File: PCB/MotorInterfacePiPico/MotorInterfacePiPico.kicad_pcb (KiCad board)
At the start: 2 copper layers, 120.2 x 65.5 mm, 47 parts, among them J1 Motor Connector, J2 Screw_Terminal_01x06, Q1 2N3904, Q2 2N3904, Q3 2N3904, U1 Pico, U2 OPA4197, U3 LM7810, U4 LM79L05

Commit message: PCB layout complete, need to DNC, need BOM
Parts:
- added G***: LOGO, TJR:gnome, B.Cu at (122.3, 105.8)
- added REF**: TNT, TSL:TNT, F.Cu at (122.2, 62.8)
- added REF**: BennyHead, TSL:BennyHead, F.Cu at (158.5, 83.0)
- added REF**: BennySmall, TSL:BennySmall, F.Cu at (162.5, 87.2)
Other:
- board text added: "A"
- board text added: "B"
- board text added: "E+"
- board text added: "E-"
- board text added: "Gnd"
- board text added: "Lim"
- board text added: "M+"
- board text added: "M-"
- board text added: "P10x"
- board text added: "Pos"
- board text added: "Spd"
- board text added: "V+"

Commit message: Layout complete, need BOM
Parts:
- U2: footprint Package_SO:SOIC-14_3.9x8.7mm_P1.27mm -> TJR:D14_TEX
- moved REF** 28.6 mm to (99.8, 80.5)
- moved G*** 23.7 mm to (99.7, 98.4)
- moved REF** 15.4 mm to (143.1, 82.8)
- moved REF** 0.66 mm to (162.7, 86.6)

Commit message: add gerbers, need BOM
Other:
- board text added: "0.0000 mm / 0.0000 mm"
- board text added: "0.3000 mm"
- board text added: "1.6000 mm"
- board text added: "120.2500 mm x 65.5000 mm"
- board text added: "2"
- board text added: "BOARD CHARACTERISTICS"
- board text added: "Board Thickness:"
- board text added: "Board overall dimensions:"
- board text added: "Castellated pads:"
- board text added: "Copper Finish:"
- board text added: "Copper Layer Count:"
- board text added: "Edge card connectors:"
- board text added: "Impedance Control:"
- board text added: "Min hole diameter:"
- board text added: "Min track/spacing:"
- board text added: "No"
- board text added: "None"
- board text added: "Plated Board Edge:"

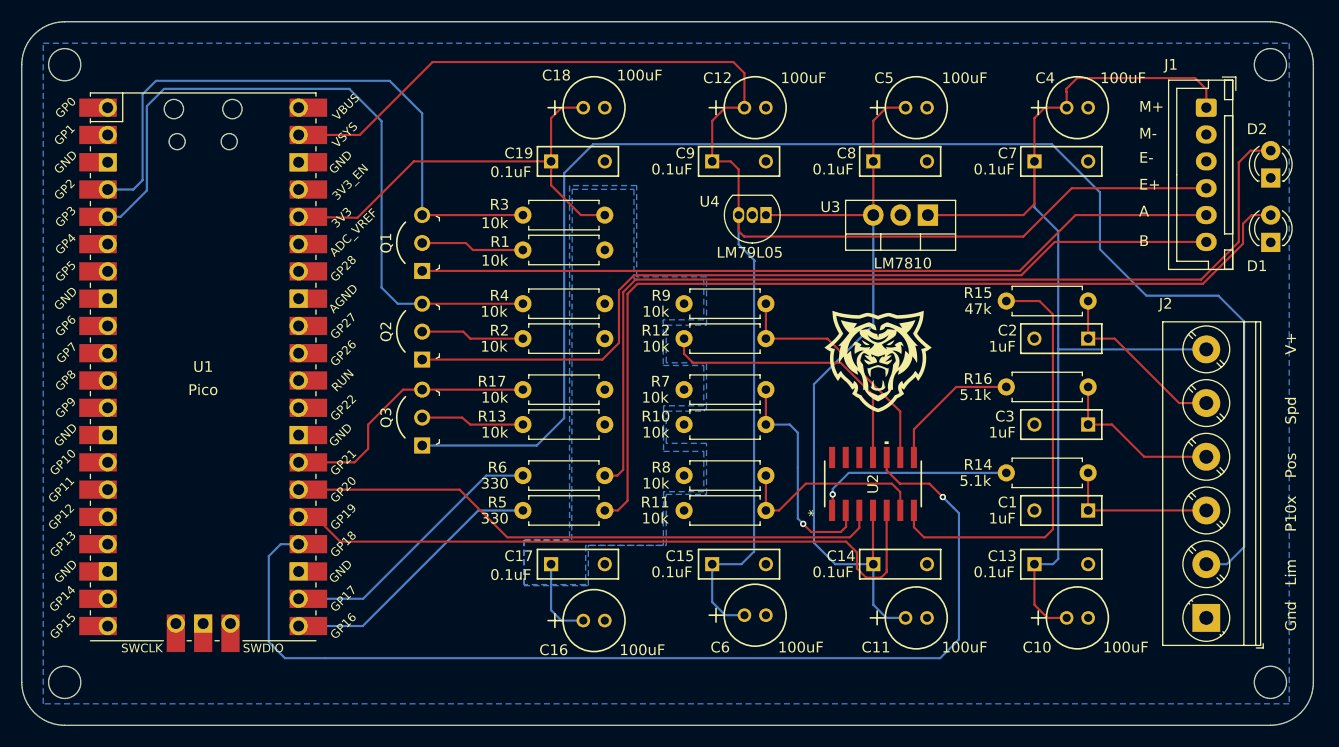
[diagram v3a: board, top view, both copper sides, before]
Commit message: Surface Mount Board design
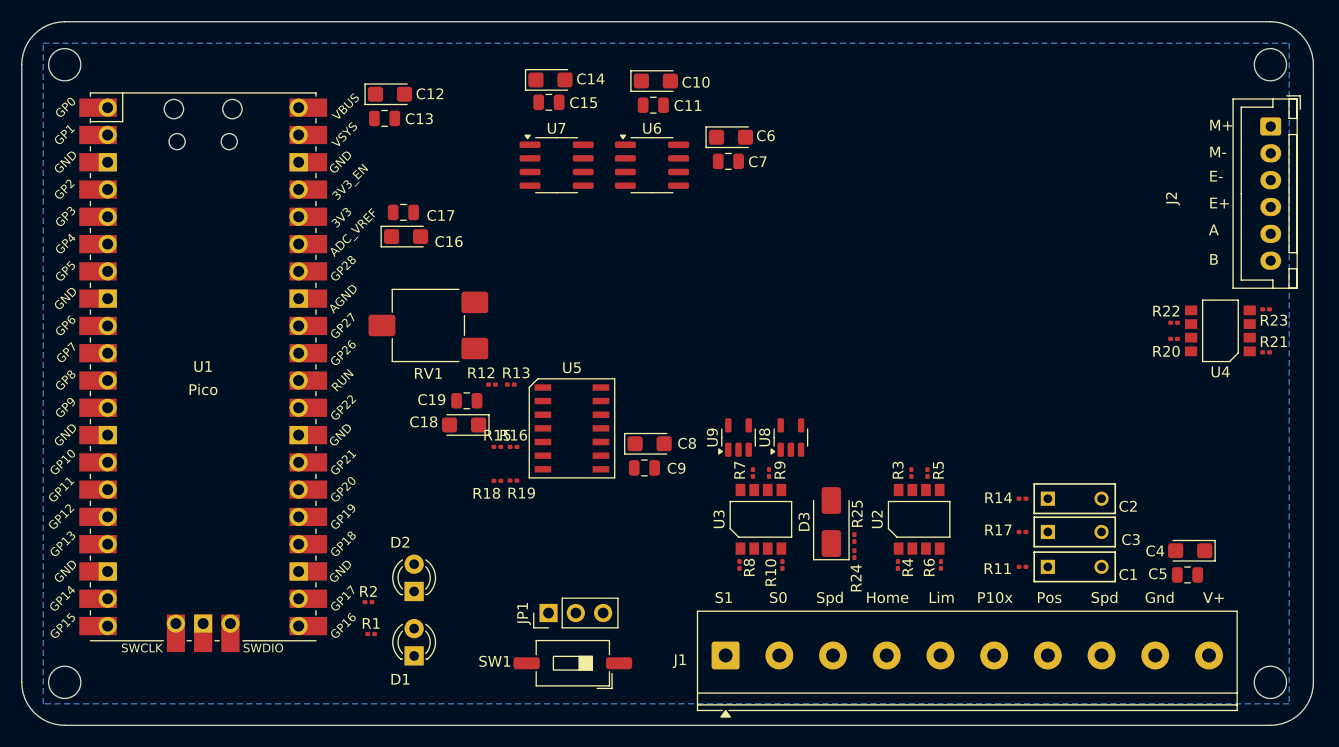
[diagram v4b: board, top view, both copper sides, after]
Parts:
- removed Q1, Q2, Q3: 2N3904, TJR:TO-92-3_Formed_Leads
- removed REF**: BennyHead, TSL:BennyHead
- removed REF**: BennySmall, TSL:BennySmall
- removed REF**: TNT, TSL:TNT
- added D3: 3.6V, Diode_SMD:D_SMA, F.Cu at (158.4, 101.6)
- added JP1: Jumper_3_Bridged12, Connector_PinHeader_2.54mm:PinHeader_1x03_P2.54mm_Vertical, F.Cu at (132.0, 110.0)
- added R18: 10k, Resistor_SMD:R_0201_0603Metric, F.Cu at (127.3, 97.7)
- added R19: 10k, Resistor_SMD:R_0201_0603Metric, F.Cu at (128.8, 97.7)
- added R20: 10k, Resistor_SMD:R_0201_0603Metric, F.Cu at (190.3, 84.5)
- added R21: 4.7k, Resistor_SMD:R_0201_0603Metric, F.Cu at (198.8, 85.8)
- added R22: 10k, Resistor_SMD:R_0201_0603Metric, F.Cu at (190.3, 83.0)
- added R23: 4.7k, Resistor_SMD:R_0201_0603Metric, F.Cu at (198.8, 81.8)
- added R24: 6.2k, Resistor_SMD:R_0201_0603Metric, F.Cu at (160.5, 104.6)
- added R25: 13k, Resistor_SMD:R_0201_0603Metric, F.Cu at (160.5, 103.1)
- added RV1: 10k, Potentiometer_SMD:Potentiometer_ACP_CA6-VSMD_Vertical, F.Cu at (120.9, 83.3)
- added SW1: SW_DIP_x01, Button_Switch_SMD:SW_DIP_SPSTx01_Slide_6.7x4.1mm_W8.61mm_P2.54mm_LowProfile, F.Cu at (134.3, 114.7)
- added U5: OPA4197, CustomBPA:SO-14_5.4_P1.27, F.Cu at (134.2, 92.9)
- added U6: LM7810, Package_SO:SOIC-8_3.9x4.9mm_P1.27mm, F.Cu at (141.7, 68.4)
- added U7: LM78L05_SO8, Package_SO:SOIC-8_3.9x4.9mm_P1.27mm, F.Cu at (132.8, 68.4)
- added U8: 74LVC1G08GV, Package_TO_SOT_SMD:SOT-23-5, F.Cu at (154.6, 93.7)
- added U9: 74LVC1G08GV, Package_TO_SOT_SMD:SOT-23-5, F.Cu at (149.7, 93.7)
- C10, C12, C16, C18, C4, C6: footprint TJR:C_Radial_D5.00mm_H12.5mm_P2.00mm -> Capacitor_Tantalum_SMD:CP_EIA-3216-10_Kemet-I
- C11, C5: value 100uF -> 0.1uF; footprint TJR:C_Radial_D5.00mm_H12.5mm_P2.00mm -> Capacitor_SMD:C_0805_2012Metric
- C13, C15, C17, C19, C7, C9: footprint TJR:C_Rect_L7.3mm_W2.5_H6.5mm_P5.0mm -> Capacitor_SMD:C_0805_2012Metric
- C14, C8: value 0.1uF -> 100uF; footprint TJR:C_Rect_L7.3mm_W2.5_H6.5mm_P5.0mm -> Capacitor_Tantalum_SMD:CP_EIA-3216-10_Kemet-I
- J1: value Motor Connector -> Screw_Terminal_01x10; footprint Connector_JST:JST_XH_B6B-XH-A_1x06_P2.50mm_Vertical -> TerminalBlock_Phoenix:TerminalBlock_Phoenix_PT-1,5-10-5.0-H_1x10_P5.00mm_Horizontal
- J2: value Screw_Terminal_01x06 -> Motor Connector; footprint TerminalBlock_Phoenix:TerminalBlock_Phoenix_PT-1,5-6-5.0-H_1x06_P5.00mm_Horizontal -> Connector_JST:JST_XH_B6B-XH-A_1x06_P2.50mm_Vertical
- R1, R2: value 10k -> 330; footprint TJR:R_Axial_DIN0207_L6.3mm_D2.5mm_P7.62mm_Horizontal -> Resistor_SMD:R_0201_0603Metric
- R10, R4, R8: value 10k -> 4.7k; footprint TJR:R_Axial_DIN0207_L6.3mm_D2.5mm_P7.62mm_Horizontal -> Resistor_SMD:R_0201_0603Metric
- R11, R17: value 10k -> 5.1k; footprint TJR:R_Axial_DIN0207_L6.3mm_D2.5mm_P7.62mm_Horizontal -> Resistor_SMD:R_0201_0603Metric
- R12, R13, R3, R7, R9: footprint TJR:R_Axial_DIN0207_L6.3mm_D2.5mm_P7.62mm_Horizontal -> Resistor_SMD:R_0201_0603Metric
- R14: value 5.1k -> 47k; footprint TJR:R_Axial_DIN0207_L6.3mm_D2.5mm_P7.62mm_Horizontal -> Resistor_SMD:R_0201_0603Metric
- R15: value 47k -> 10k; footprint TJR:R_Axial_DIN0207_L6.3mm_D2.5mm_P7.62mm_Horizontal -> Resistor_SMD:R_0201_0603Metric
- R16: value 5.1k -> 10k; footprint TJR:R_Axial_DIN0207_L6.3mm_D2.5mm_P7.62mm_Horizontal -> Resistor_SMD:R_0201_0603Metric
- R5: value 330 -> 10k; footprint TJR:R_Axial_DIN0207_L6.3mm_D2.5mm_P7.62mm_Horizontal -> Resistor_SMD:R_0201_0603Metric
- R6: value 330 -> 4.7k; footprint TJR:R_Axial_DIN0207_L6.3mm_D2.5mm_P7.62mm_Horizontal -> Resistor_SMD:R_0201_0603Metric
- U2: value OPA4197 -> ILD217T; footprint TJR:D14_TEX -> CustomBPA:SOIC-8_5.46mm_P1.27
- U3: value LM7810 -> ILD217T; footprint Package_TO_SOT_THT:TO-220-3_Vertical -> CustomBPA:SOIC-8_5.46mm_P1.27
- U4: value LM79L05 -> ILD217T; footprint Package_TO_SOT_THT:TO-92_Inline -> CustomBPA:SOIC-8_5.46mm_P1.27
- moved D1 88.6 mm to (119.5, 114.0)
- moved D2 88.6 mm to (119.5, 108.0)
- moved C13 73.4 mm to (116.8, 64.0)
- moved J1 67.8 mm to (148.5, 114.0), turned to 0 degrees
- moved C10 62.9 mm to (142.0, 60.5)
- moved C14 54.2 mm to (132.2, 60.4)
- moved C11 53.2 mm to (141.8, 62.8)
- moved C5 50.8 mm to (191.5, 106.5), turned to 180 degrees
- moved R15 49.3 mm to (127.3, 94.6)
- moved R16 46.2 mm to (128.8, 94.6)
- moved J2 46.1 mm to (199.3, 64.8), turned to -90 degrees
- moved C15 45.6 mm to (132.1, 62.5)
- moved C6 44.5 mm to (149.0, 65.8)
- moved U4 43.7 mm to (194.6, 83.8), turned to 90 degrees
- moved C4 42.8 mm to (191.8, 104.2), turned to 180 degrees
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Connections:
- C10 pad 1: +12V -> +10V
- C13 pad 1: +12V -> +5V
- C14 pad 1: +10V -> +5V
- C4 pad 1: +12V -> +Motor_Sup
- C5 pad 1: +10V -> +Motor_Sup
- C6 pad 1: +5V -> +Motor_Sup
- C7 pad 1: +12V -> +Motor_Sup
- C9 pad 1: +5V -> +10V
- J1 pad 1: +12V -> Net-(J1-Pin_1)
- J1 pad 2: GND -> Net-(J1-Pin_2)
- J1 pad 3: GND -> Speed Set
- J1 pad 4: +5V -> Net-(J1-Pin_4)
- J1 pad 5: A -> Net-(J1-Pin_5)
- J1 pad 6: B -> Analog Position x10
- J2 pad 1: GND -> M+
- J2 pad 2: Net-(J2-Pin_2) -> GND
- J2 pad 3: Analog Position x10 -> GND
- J2 pad 4: Analog Position -> +5V
- J2 pad 5: Analog Speed -> Net-(J2-Pin_5)
- J2 pad 6: +12V -> Net-(J2-Pin_6)
- R1 pad 1: +3.3V -> Net-(U1-GPIO16)
- R1 pad 2: Net-(Q1-B) -> Net-(D1-A)
- R10 pad 1: Net-(U2A--) -> Net-(J1-Pin_2)
- R10 pad 2: GND -> Net-(R10-Pad2)
- R11 pad 1: Net-(U2B--) -> Net-(R11-Pad1)
- R11 pad 2: GND -> Analog Position x10
- R12 pad 1: Net-(U2C--) -> +3.3V
- R12 pad 2: GND -> Net-(U5A--)
- R13 pad 1: +3.3V -> Net-(U5A--)
- R13 pad 2: Net-(Q3-B) -> GND
- R14 pad 2: Analog Position x10 -> Analog Speed
- R15 pad 1: Net-(R15-Pad1) -> +3.3V
- R15 pad 2: Analog Speed -> Net-(U5B--)
- R16 pad 1: Net-(R16-Pad1) -> Net-(U5B--)
- R16 pad 2: Analog Position -> GND
- R17 pad 1: +3.3V -> Net-(R17-Pad1)
- R17 pad 2: Limit Switch -> Analog Position
- R2 pad 1: +3.3V -> Net-(U1-GPIO17)
- R2 pad 2: Net-(Q2-B) -> Net-(D2-A)
- R3 pad 2: Net-(Q1-C) -> Home
- R4 pad 1: +3.3V -> Net-(J1-Pin_4)
- R4 pad 2: Net-(Q2-C) -> Net-(R4-Pad2)
- R5 pad 1: Net-(U1-GPIO16) -> +3.3V
- R5 pad 2: Net-(D1-A) -> Limit Switch
- R6 pad 1: Net-(U1-GPIO17) -> Net-(J1-Pin_5)
- R6 pad 2: Net-(D2-A) -> Net-(R6-Pad2)
- R7 pad 2: Net-(U2A--) -> S1
- R8 pad 1: +3.3V -> Net-(J1-Pin_1)
- R8 pad 2: Net-(U2B--) -> Net-(R8-Pad2)
- R9 pad 2: Net-(U2C--) -> S0
- U1 pad 17: unconnected-(U1-GPIO13-Pad17) -> Net-(U1-GPIO13)
- U1 pad 19: unconnected-(U1-GPIO14-Pad19) -> Limit Switch
- U1 pad 20: unconnected-(U1-GPIO15-Pad20)_0 -> Home
- U1 pad 27: Limit Switch -> Speed PWM
- U1 pad 31: unconnected-(U1-GPIO26_ADC0-Pad31) -> Net-(D3-K)
- U1 pad 32: unconnected-(U1-GPIO27_ADC1-Pad32)_0 -> Net-(U1-GPIO27_ADC1)
- U1 pad 4: Net-(Q1-C) -> A
- U1 pad 5: Net-(Q2-C) -> B
- U2 pad 1: Net-(R14-Pad1) -> Net-(R4-Pad2)
- U2 pad 2: Net-(U2A--) -> GND_PLC
- U2 pad 3: PWM Position x10 -> GND_PLC
- U2 pad 4: +10V -> Net-(R6-Pad2)
- U2 pad 5: PWM Speed -> GND
- U2 pad 6: Net-(U2B--) -> Limit Switch
- U2 pad 7: Net-(R15-Pad1) -> Home
- U2 pad 8: Net-(R16-Pad1) -> GND
- U3 pad 1: +12V -> Net-(R8-Pad2)
- U3 pad 2: GND -> GND_PLC
- U3 pad 3: +10V -> GND_PLC
- U4 pad 1: +10V -> Net-(R21-Pad2)
- U4 pad 3: +5V -> GND
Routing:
- net +5V: track 152.8 -> 0.00 mm
- net Net-(J2-Pin_2): track 136.6 -> 0.00 mm
- net +12V: track 100.5 -> 0.00 mm
- net PWM Position: track 98.2 -> 0.00 mm, vias 1 -> 0
- net Net-(D2-A): track 88.6 -> 0.00 mm
- net Net-(D1-A): track 85.8 -> 0.00 mm
- net B: track 80.4 -> 0.00 mm
- net A: track 75.2 -> 0.00 mm
- net +10V: track 73.7 -> 0.00 mm
- net Net-(Q2-C): track 65.6 -> 0.00 mm
- net PWM Speed: track 63.9 -> 0.00 mm
- net Net-(Q1-C): track 58.3 -> 0.00 mm
- net PWM Position x10: track 56.0 -> 0.00 mm
- net +3.3V: track 49.2 -> 0.00 mm
- net Net-(R15-Pad1): track 40.1 -> 0.00 mm
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- removed copper zone on B.Cu, net +3.3V
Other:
- board text added: "Home"
- board text added: "S0"
- board text added: "S1"

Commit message: Made new Anderson PCB project and reverted Tim R's folder
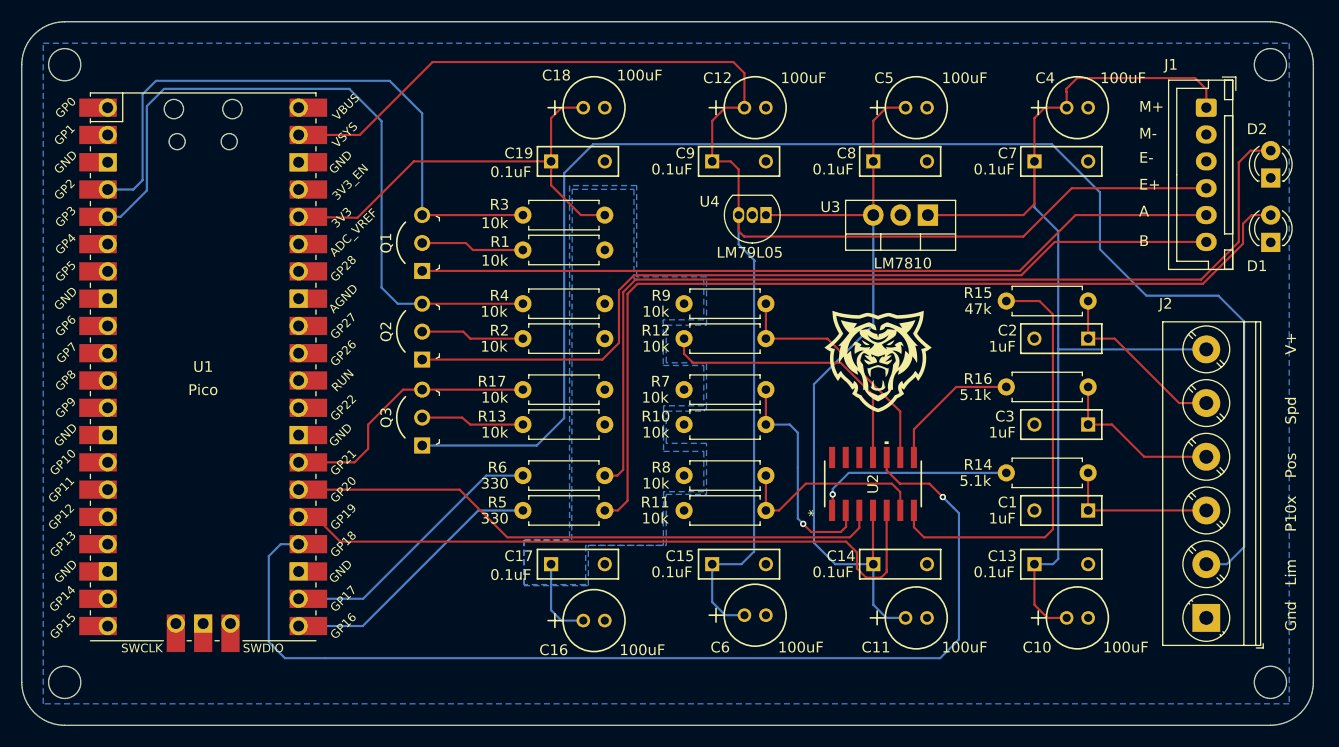
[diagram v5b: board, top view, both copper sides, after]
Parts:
- removed D3: 3.6V, Diode_SMD:D_SMA
- removed JP1: Jumper_3_Bridged12, Connector_PinHeader_2.54mm:PinHeader_1x03_P2.54mm_Vertical
- removed R18, R19, R20, R22: 10k, Resistor_SMD:R_0201_0603Metric
- removed R21, R23: 4.7k, Resistor_SMD:R_0201_0603Metric
- removed R24: 6.2k, Resistor_SMD:R_0201_0603Metric
- removed R25: 13k, Resistor_SMD:R_0201_0603Metric
- removed RV1: 10k, Potentiometer_SMD:Potentiometer_ACP_CA6-VSMD_Vertical
- removed SW1: SW_DIP_x01, Button_Switch_SMD:SW_DIP_SPSTx01_Slide_6.7x4.1mm_W8.61mm_P2.54mm_LowProfile
- removed U5: OPA4197, CustomBPA:SO-14_5.4_P1.27
- removed U6: LM7810, Package_SO:SOIC-8_3.9x4.9mm_P1.27mm
- removed U7: LM78L05_SO8, Package_SO:SOIC-8_3.9x4.9mm_P1.27mm
- removed U8, U9: 74LVC1G08GV, Package_TO_SOT_SMD:SOT-23-5
- added Q1: 2N3904, TJR:TO-92-3_Formed_Leads, F.Cu at (120.3, 78.2)
- added Q2: 2N3904, TJR:TO-92-3_Formed_Leads, F.Cu at (120.3, 86.5)
- added Q3: 2N3904, TJR:TO-92-3_Formed_Leads, F.Cu at (120.3, 94.5)
- added REF**: BennyHead, TSL:BennyHead, F.Cu at (143.1, 82.8)
- added REF**: BennySmall, TSL:BennySmall, F.Cu at (162.7, 86.6)
- added REF**: TNT, TSL:TNT, F.Cu at (99.8, 80.5)
- C10, C12, C16, C18, C4, C6: footprint Capacitor_Tantalum_SMD:CP_EIA-3216-10_Kemet-I -> TJR:C_Radial_D5.00mm_H12.5mm_P2.00mm
- C11, C5: value 0.1uF -> 100uF; footprint Capacitor_SMD:C_0805_2012Metric -> TJR:C_Radial_D5.00mm_H12.5mm_P2.00mm
- C13, C15, C17, C19, C7, C9: footprint Capacitor_SMD:C_0805_2012Metric -> TJR:C_Rect_L7.3mm_W2.5_H6.5mm_P5.0mm
- C14, C8: value 100uF -> 0.1uF; footprint Capacitor_Tantalum_SMD:CP_EIA-3216-10_Kemet-I -> TJR:C_Rect_L7.3mm_W2.5_H6.5mm_P5.0mm
- J1: value Screw_Terminal_01x10 -> Motor Connector; footprint TerminalBlock_Phoenix:TerminalBlock_Phoenix_PT-1,5-10-5.0-H_1x10_P5.00mm_Horizontal -> Connector_JST:JST_XH_B6B-XH-A_1x06_P2.50mm_Vertical
- J2: value Motor Connector -> Screw_Terminal_01x06; footprint Connector_JST:JST_XH_B6B-XH-A_1x06_P2.50mm_Vertical -> TerminalBlock_Phoenix:TerminalBlock_Phoenix_PT-1,5-6-5.0-H_1x06_P5.00mm_Horizontal
- R1, R2: value 330 -> 10k; footprint Resistor_SMD:R_0201_0603Metric -> TJR:R_Axial_DIN0207_L6.3mm_D2.5mm_P7.62mm_Horizontal
- R10, R4, R8: value 4.7k -> 10k; footprint Resistor_SMD:R_0201_0603Metric -> TJR:R_Axial_DIN0207_L6.3mm_D2.5mm_P7.62mm_Horizontal
- R11, R17: value 5.1k -> 10k; footprint Resistor_SMD:R_0201_0603Metric -> TJR:R_Axial_DIN0207_L6.3mm_D2.5mm_P7.62mm_Horizontal
- R12, R13, R3, R7, R9: footprint Resistor_SMD:R_0201_0603Metric -> TJR:R_Axial_DIN0207_L6.3mm_D2.5mm_P7.62mm_Horizontal
- R14: value 47k -> 5.1k; footprint Resistor_SMD:R_0201_0603Metric -> TJR:R_Axial_DIN0207_L6.3mm_D2.5mm_P7.62mm_Horizontal
- R15: value 10k -> 47k; footprint Resistor_SMD:R_0201_0603Metric -> TJR:R_Axial_DIN0207_L6.3mm_D2.5mm_P7.62mm_Horizontal
- R16: value 10k -> 5.1k; footprint Resistor_SMD:R_0201_0603Metric -> TJR:R_Axial_DIN0207_L6.3mm_D2.5mm_P7.62mm_Horizontal
- R5: value 10k -> 330; footprint Resistor_SMD:R_0201_0603Metric -> TJR:R_Axial_DIN0207_L6.3mm_D2.5mm_P7.62mm_Horizontal
- R6: value 4.7k -> 330; footprint Resistor_SMD:R_0201_0603Metric -> TJR:R_Axial_DIN0207_L6.3mm_D2.5mm_P7.62mm_Horizontal
- U2: value ILD217T -> OPA4197; footprint CustomBPA:SOIC-8_5.46mm_P1.27 -> TJR:D14_TEX
- U3: value ILD217T -> LM7810; footprint CustomBPA:SOIC-8_5.46mm_P1.27 -> Package_TO_SOT_THT:TO-220-3_Vertical
- U4: value ILD217T -> LM79L05; footprint CustomBPA:SOIC-8_5.46mm_P1.27 -> Package_TO_SOT_THT:TO-92_Inline
- moved D1 88.6 mm to (199.3, 75.5)
- moved D2 88.6 mm to (199.3, 69.5)
- moved C13 73.4 mm to (177.3, 105.5)
- moved J1 67.8 mm to (193.3, 63.0), turned to -90 degrees
- moved C10 62.9 mm to (180.3, 110.5)
- moved C14 54.2 mm to (162.3, 105.5)
- moved C11 53.2 mm to (165.3, 110.5)
- moved C5 50.8 mm to (165.3, 63.0), turned to 0 degrees
- moved R15 49.3 mm to (174.7, 81.0)
- moved R16 46.2 mm to (174.7, 89.0)
- moved J2 46.1 mm to (193.3, 110.5), turned to 90 degrees
- moved C15 45.6 mm to (147.3, 105.5)
- moved C6 44.5 mm to (150.3, 110.2)
- moved U4 43.7 mm to (152.3, 73.0), turned to 180 degrees
- moved C4 42.8 mm to (180.3, 63.0), turned to 0 degrees
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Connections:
- C10 pad 1: +10V -> +12V
- C13 pad 1: +5V -> +12V
- C14 pad 1: +5V -> +10V
- C4 pad 1: +Motor_Sup -> +12V
- C5 pad 1: +Motor_Sup -> +10V
- C6 pad 1: +Motor_Sup -> +5V
- C7 pad 1: +Motor_Sup -> +12V
- C9 pad 1: +10V -> +5V
- J1 pad 1: Net-(J1-Pin_1) -> +12V
- J1 pad 2: Net-(J1-Pin_2) -> GND
- J1 pad 3: Speed Set -> GND
- J1 pad 4: Net-(J1-Pin_4) -> +5V
- J1 pad 5: Net-(J1-Pin_5) -> A
- J1 pad 6: Analog Position x10 -> B
- J2 pad 1: M+ -> GND
- J2 pad 2: GND -> Net-(J2-Pin_2)
- J2 pad 3: GND -> Analog Position x10
- J2 pad 4: +5V -> Analog Position
- J2 pad 5: Net-(J2-Pin_5) -> Analog Speed
- J2 pad 6: Net-(J2-Pin_6) -> +12V
- R1 pad 1: Net-(U1-GPIO16) -> +3.3V
- R1 pad 2: Net-(D1-A) -> Net-(Q1-B)
- R10 pad 1: Net-(J1-Pin_2) -> Net-(U2A--)
- R10 pad 2: Net-(R10-Pad2) -> GND
- R11 pad 1: Net-(R11-Pad1) -> Net-(U2B--)
- R11 pad 2: Analog Position x10 -> GND
- R12 pad 1: +3.3V -> Net-(U2C--)
- R12 pad 2: Net-(U5A--) -> GND
- R13 pad 1: Net-(U5A--) -> +3.3V
- R13 pad 2: GND -> Net-(Q3-B)
- R14 pad 2: Analog Speed -> Analog Position x10
- R15 pad 1: +3.3V -> Net-(R15-Pad1)
- R15 pad 2: Net-(U5B--) -> Analog Speed
- R16 pad 1: Net-(U5B--) -> Net-(R16-Pad1)
- R16 pad 2: GND -> Analog Position
- R17 pad 1: Net-(R17-Pad1) -> +3.3V
- R17 pad 2: Analog Position -> Limit Switch
- R2 pad 1: Net-(U1-GPIO17) -> +3.3V
- R2 pad 2: Net-(D2-A) -> Net-(Q2-B)
- R3 pad 2: Home -> Net-(Q1-C)
- R4 pad 1: Net-(J1-Pin_4) -> +3.3V
- R4 pad 2: Net-(R4-Pad2) -> Net-(Q2-C)
- R5 pad 1: +3.3V -> Net-(U1-GPIO16)
- R5 pad 2: Limit Switch -> Net-(D1-A)
- R6 pad 1: Net-(J1-Pin_5) -> Net-(U1-GPIO17)
- R6 pad 2: Net-(R6-Pad2) -> Net-(D2-A)
- R7 pad 2: S1 -> Net-(U2A--)
- R8 pad 1: Net-(J1-Pin_1) -> +3.3V
- R8 pad 2: Net-(R8-Pad2) -> Net-(U2B--)
- R9 pad 2: S0 -> Net-(U2C--)
- U1 pad 17: Net-(U1-GPIO13) -> unconnected-(U1-GPIO13-Pad17)
- U1 pad 19: Limit Switch -> unconnected-(U1-GPIO14-Pad19)
- U1 pad 20: Home -> unconnected-(U1-GPIO15-Pad20)_0
- U1 pad 27: Speed PWM -> Limit Switch
- U1 pad 31: Net-(D3-K) -> unconnected-(U1-GPIO26_ADC0-Pad31)
- U1 pad 32: Net-(U1-GPIO27_ADC1) -> unconnected-(U1-GPIO27_ADC1-Pad32)_0
- U1 pad 4: A -> Net-(Q1-C)
- U1 pad 5: B -> Net-(Q2-C)
- U2 pad 1: Net-(R4-Pad2) -> Net-(R14-Pad1)
- U2 pad 2: GND_PLC -> Net-(U2A--)
- U2 pad 3: GND_PLC -> PWM Position x10
- U2 pad 4: Net-(R6-Pad2) -> +10V
- U2 pad 5: GND -> PWM Speed
- U2 pad 6: Limit Switch -> Net-(U2B--)
- U2 pad 7: Home -> Net-(R15-Pad1)
- U2 pad 8: GND -> Net-(R16-Pad1)
- U3 pad 1: Net-(R8-Pad2) -> +12V
- U3 pad 2: GND_PLC -> GND
- U3 pad 3: GND_PLC -> +10V
- U4 pad 1: Net-(R21-Pad2) -> +10V
- U4 pad 3: GND -> +5V
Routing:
- net +5V: track 0.00 -> 152.8 mm
- net Net-(J2-Pin_2): track 0.00 -> 136.6 mm
- net +12V: track 0.00 -> 100.5 mm
- net PWM Position: track 0.00 -> 98.2 mm, vias 0 -> 1
- net Net-(D2-A): track 0.00 -> 88.6 mm
- net Net-(D1-A): track 0.00 -> 85.8 mm
- net B: track 0.00 -> 80.4 mm
- net A: track 0.00 -> 75.2 mm
- net +10V: track 0.00 -> 73.7 mm
- net Net-(Q2-C): track 0.00 -> 65.6 mm
- net PWM Speed: track 0.00 -> 63.9 mm
- net Net-(Q1-C): track 0.00 -> 58.3 mm
- net PWM Position x10: track 0.00 -> 56.0 mm
- net +3.3V: track 0.00 -> 49.2 mm
- net Net-(R15-Pad1): track 0.00 -> 40.1 mm
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- added copper zone on B.Cu, net +3.3V
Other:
- board text removed: "Home"
- board text removed: "S0"
- board text removed: "S1"
